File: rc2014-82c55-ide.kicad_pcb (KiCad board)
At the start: 2 copper layers, 100 x 50 mm, 23 parts, among them J1 Conn_01x02, J2 Conn_02x20_Odd_Even, J3 Conn_02x22_Odd_Even, J5 Conn_01x02, P1 Conn_01x39, SW1 SW_DIP_x06, U1 82C55A_PLCC, U2 74HCT688, U3 74HCT04

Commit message: Update PCB components
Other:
- rule pad_to_mask_clearance: 0.2 -> 0
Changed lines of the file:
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@@
   (title_block
     (title "RC2014 82c55 IDE adapter")
-    (date "2022-03-09")
+    (date "2022-10-17")
     (rev "3-pre")
   )
@@
   )
   (setup
-    (pad_to_mask_clearance 0.2)
+    (pad_to_mask_clearance 0)
     (pcbplotparams
       (layerselection 0x00010f0_ffffffff)
@@
     (descr "Through hole straight pin header, 1x39, 2.54mm pitch, single row")
     (tags "Through hole pin header THT 1x39 2.54mm single row")
-    (property "Sheetfile" "rc2014-82c55-ide.kicad_sch")
+    (property "Sheetfile" "File: rc2014-82c55-ide.kicad_sch")
     (property "Sheetname" "")
     (attr through_hole)
@@
     (descr "PLCC, 44 pins, through hole")
     (tags "plcc leaded")
-    (property "Sheetfile" "rc2014-82c55-ide.kicad_sch")
+    (property "Sheetfile" "File: rc2014-82c55-ide.kicad_sch")
     (property "Sheetname" "")
     (attr through_hole)
@@
     (descr "Resistor, Axial_DIN0207 series, Axial, Horizontal, pin pitch=7.62mm, 0.25W = 1/4W, length*diameter=6.3*2.5mm^2, http://cdn-reichelt.de/documents/datenblatt/B400/1_4W%23YAG.pdf")
     (tags "Resistor Axial_DIN0207 series Axial Horizontal pin pitch 7.62mm 0.25W = 1/4W length 6.3mm diameter 2.5mm")
-    (property "Sheetfile" "rc2014-82c55-ide.kicad_sch")
+    (property "Sheetfile" "File: rc2014-82c55-ide.kicad_sch")
     (property "Sheetname" "")
     (attr through_hole)
@@
     (descr "20-lead though-hole mounted DIP package, row spacing 7.62 mm (300 mils), Socket, LongPads")
     (tags "THT DIP DIL PDIP 2.54mm 7.62mm 300mil Socket LongPads")
-    (property "Sheetfile" "rc2014-82c55-ide.kicad_sch")
+    (property "Sheetfile" "File: rc2014-82c55-ide.kicad_sch")
     (property "Sheetname" "")
     (attr through_hole)
@@
     (descr "14-lead though-hole mounted DIP package, row spacing 7.62 mm (300 mils), Socket, LongPads")
     (tags "THT DIP DIL PDIP 2.54mm 7.62mm 300mil Socket LongPads")
-    (property "Sheetfile" "rc2014-82c55-ide.kicad_sch")
+    (property "Sheetfile" "File: rc2014-82c55-ide.kicad_sch")
     (property "Sheetname" "")
     (attr through_hole)
@@
     (descr "Through hole straight pin header, 2x22, 2.00mm pitch, double rows")
     (tags "Through hole pin header THT 2x22 2.00mm double row")
-    (property "Sheetfile" "rc2014-82c55-ide.kicad_sch")
+    (property "Sheetfile" "File: rc2014-82c55-ide.kicad_sch")
     (property "Sheetname" "")
     (attr through_hole)
@@
     (descr "6x-dip-switch SPST , Slide, row spacing 7.62 mm (300 mils), body size 9.78x17.42mm (see e.g. https://www.ctscorp.com/wp-content/uploads/206-208.pdf)")
     (tags "DIP Switch SPST Slide 7.62mm 300mil")
-    (property "Sheetfile" "rc2014-82c55-ide.kicad_sch")
+    (property "Sheetfile" "File: rc2014-82c55-ide.kicad_sch")
     (property "Sheetname" "")
     (attr through_hole)
@@
     (descr "C, Disc series, Radial, pin pitch=2.50mm, , diameter*width=3*2mm^2, Capacitor")
     (tags "C Disc series Radial pin pitch 2.50mm  diameter 3mm width 2mm Capacitor")
-    (property "Sheetfile" "rc2014-82c55-ide.kicad_sch")
+    (property "Sheetfile" "File: rc2014-82c55-ide.kicad_sch")
     (property "Sheetname" "")
     (attr through_hole)
@@
     (descr "C, Disc series, Radial, pin pitch=2.50mm, , diameter*width=3*2mm^2, Capacitor")
     (tags "C Disc series Radial pin pitch 2.50mm  diameter 3mm width 2mm Capacitor")
-    (property "Sheetfile" "rc2014-82c55-ide.kicad_sch")
+    (property "Sheetfile" "File: rc2014-82c55-ide.kicad_sch")
     (property "Sheetname" "")
     (attr through_hole)
@@
     (descr "C, Disc series, Radial, pin pitch=2.50mm, , diameter*width=3*2mm^2, Capacitor")
     (tags "C Disc series Radial pin pitch 2.50mm  diameter 3mm width 2mm Capacitor")
-    (property "Sheetfile" "rc2014-82c55-ide.kicad_sch")
+    (property "Sheetfile" "File: rc2014-82c55-ide.kicad_sch")
     (property "Sheetname" "")
     (attr through_hole)
@@
     (descr "Through hole straight pin header, 2x20, 2.54mm pitch, double rows")
     (tags "Through hole pin header THT 2x20 2.54mm double row")
-    (property "Sheetfile" "rc2014-82c55-ide.kicad_sch")
+    (property "Sheetfile" "File: rc2014-82c55-ide.kicad_sch")
     (property "Sheetname" "")
     (attr through_hole)
@@
     (descr "Through hole straight pin header, 1x02, 2.54mm pitch, single row")
     (tags "Through hole pin header THT 1x02 2.54mm single row")
-    (property "Sheetfile" "rc2014-82c55-ide.kicad_sch")
+    (property "Sheetfile" "File: rc2014-82c55-ide.kicad_sch")
     (property "Sheetname" "")
     (attr through_hole)
@@
     (descr "Through hole straight pin header, 1x03, 2.54mm pitch, single row")
     (tags "Through hole pin header THT 1x03 2.54mm single row")
-    (property "Sheetfile" "rc2014-82c55-ide.kicad_sch")
+    (property "Sheetfile" "File: rc2014-82c55-ide.kicad_sch")
     (property "Sheetname" "")
     (attr through_hole)
@@
     (descr "Through hole straight pin header, 1x03, 2.54mm pitch, single row")
     (tags "Through hole pin header THT 1x03 2.54mm single row")
-    (property "Sheetfile" "rc2014-82c55-ide.kicad_sch")
+    (property "Sheetfile" "File: rc2014-82c55-ide.kicad_sch")
     (property "Sheetname" "")
     (attr through_hole)
@@
     (descr "Through hole straight pin header, 1x03, 2.54mm pitch, single row")
     (tags "Through hole pin header THT 1x03 2.54mm single row")
-    (property "Sheetfile" "rc2014-82c55-ide.kicad_sch")
+    (property "Sheetfile" "File: rc2014-82c55-ide.kicad_sch")
     (property "Sheetname" "")
     (attr through_hole)
@@
     (descr "Through hole straight pin header, 1x03, 2.54mm pitch, single row")
     (tags "Through hole pin header THT 1x03 2.54mm single row")
-    (property "Sheetfile" "rc2014-82c55-ide.kicad_sch")
+    (property "Sheetfile" "File: rc2014-82c55-ide.kicad_sch")
     (property "Sheetname" "")
     (attr through_hole)
@@
     (descr "8-pin Resistor SIP pack")
     (tags "R")
-    (property "Sheetfile" "rc2014-82c55-ide.kicad_sch")
+    (property "Sheetfile" "File: rc2014-82c55-ide.kicad_sch")
     (property "Sheetname" "")
     (attr through_hole)
@@
     (descr "Resistor, Axial_DIN0207 series, Axial, Horizontal, pin pitch=7.62mm, 0.25W = 1/4W, length*diameter=6.3*2.5mm^2, http://cdn-reichelt.de/documents/datenblatt/B400/1_4W%23YAG.pdf")
     (tags "Resistor Axial_DIN0207 series Axial Horizontal pin pitch 7.62mm 0.25W = 1/4W length 6.3mm diameter 2.5mm")
-    (property "Sheetfile" "rc2014-82c55-ide.kicad_sch")
+    (property "Sheetfile" "File: rc2014-82c55-ide.kicad_sch")
     (property "Sheetname" "")
     (attr through_hole)
@@
     (descr "Resistor, Axial_DIN0207 series, Axial, Horizontal, pin pitch=7.62mm, 0.25W = 1/4W, length*diameter=6.3*2.5mm^2, http://cdn-reichelt.de/documents/datenblatt/B400/1_4W%23YAG.pdf")
     (tags "Resistor Axial_DIN0207 series Axial Horizontal pin pitch 7.62mm 0.25W = 1/4W length 6.3mm diameter 2.5mm")
-    (property "Sheetfile" "rc2014-82c55-ide.kicad_sch")
+    (property "Sheetfile" "File: rc2014-82c55-ide.kicad_sch")
     (property "Sheetname" "")
     (attr through_hole)
@@
     (descr "Resistor, Axial_DIN0207 series, Axial, Horizontal, pin pitch=7.62mm, 0.25W = 1/4W, length*diameter=6.3*2.5mm^2, http://cdn-reichelt.de/documents/datenblatt/B400/1_4W%23YAG.pdf")
     (tags "Resistor Axial_DIN0207 series Axial Horizontal pin pitch 7.62mm 0.25W = 1/4W length 6.3mm diameter 2.5mm")
-    (property "Sheetfile" "rc2014-82c55-ide.kicad_sch")
+    (property "Sheetfile" "File: rc2014-82c55-ide.kicad_sch")
     (property "Sheetname" "")
     (attr through_hole)
@@
     (descr "LED, diameter 3.0mm, 2 pins")
     (tags "LED diameter 3.0mm 2 pins")
-    (property "Sheetfile" "rc2014-82c55-ide.kicad_sch")
+    (property "Sheetfile" "File: rc2014-82c55-ide.kicad_sch")
     (property "Sheetname" "")
     (attr through_hole)
@@
     (descr "Through hole straight pin header, 1x02, 2.54mm pitch, single row")
     (tags "Through hole pin header THT 1x02 2.54mm single row")
-    (property "Sheetfile" "rc2014-82c55-ide.kicad_sch")
+    (property "Sheetfile" "File: rc2014-82c55-ide.kicad_sch")
     (property "Sheetname" "")
     (attr through_hole)
@@
     (connect_pads (clearance 0))
     (min_thickness 0.254)
-    (keepout (tracks not_allowed) (vias not_allowed) (pads allowed ) (copperpour allowed) (footprints allowed))
+    (keepout (tracks not_allowed) (vias not_allowed) (pads allowed) (copperpour allowed) (footprints allowed))
     (fill (thermal_gap 0.508) (thermal_bridge_width 0.508))
     (polygon
@@
     (connect_pads (clearance 0))
     (min_thickness 0.254)
-    (keepout (tracks not_allowed) (vias not_allowed) (pads allowed ) (copperpour allowed) (footprints allowed))
+    (keepout (tracks not_allowed) (vias not_allowed) (pads allowed) (copperpour allowed) (footprints allowed))
     (fill (thermal_gap 0.508) (thermal_bridge_width 0.508))
     (polygon
@@
     (connect_pads (clearance 0))
     (min_thickness 0.254)
-    (keepout (tracks allowed) (vias allowed) (pads allowed ) (copperpour not_allowed) (footprints allowed))
+    (keepout (tracks allowed) (vias allowed) (pads allowed) (copperpour not_allowed) (footprints allowed))
     (fill (thermal_gap 0.508) (thermal_bridge_width 0.508))
     (polygon

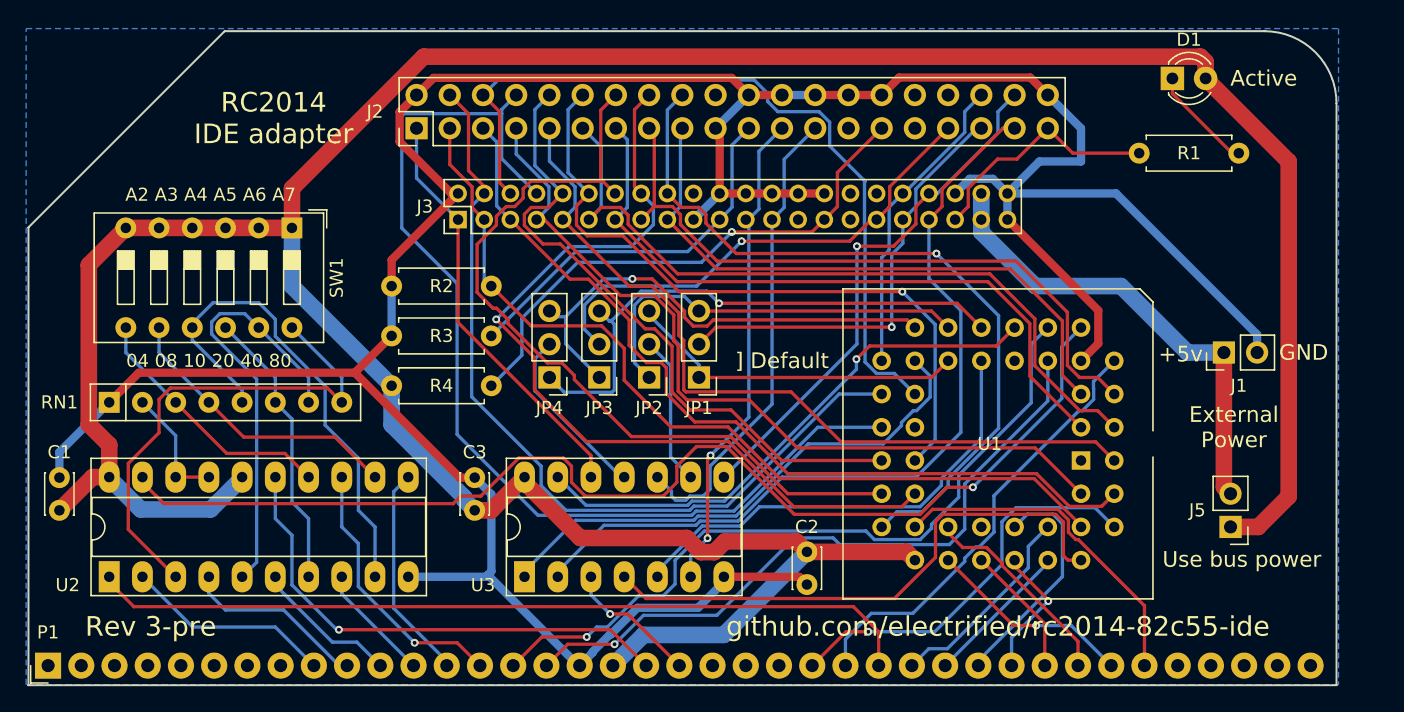
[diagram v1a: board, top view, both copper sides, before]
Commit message: update to kicad 9
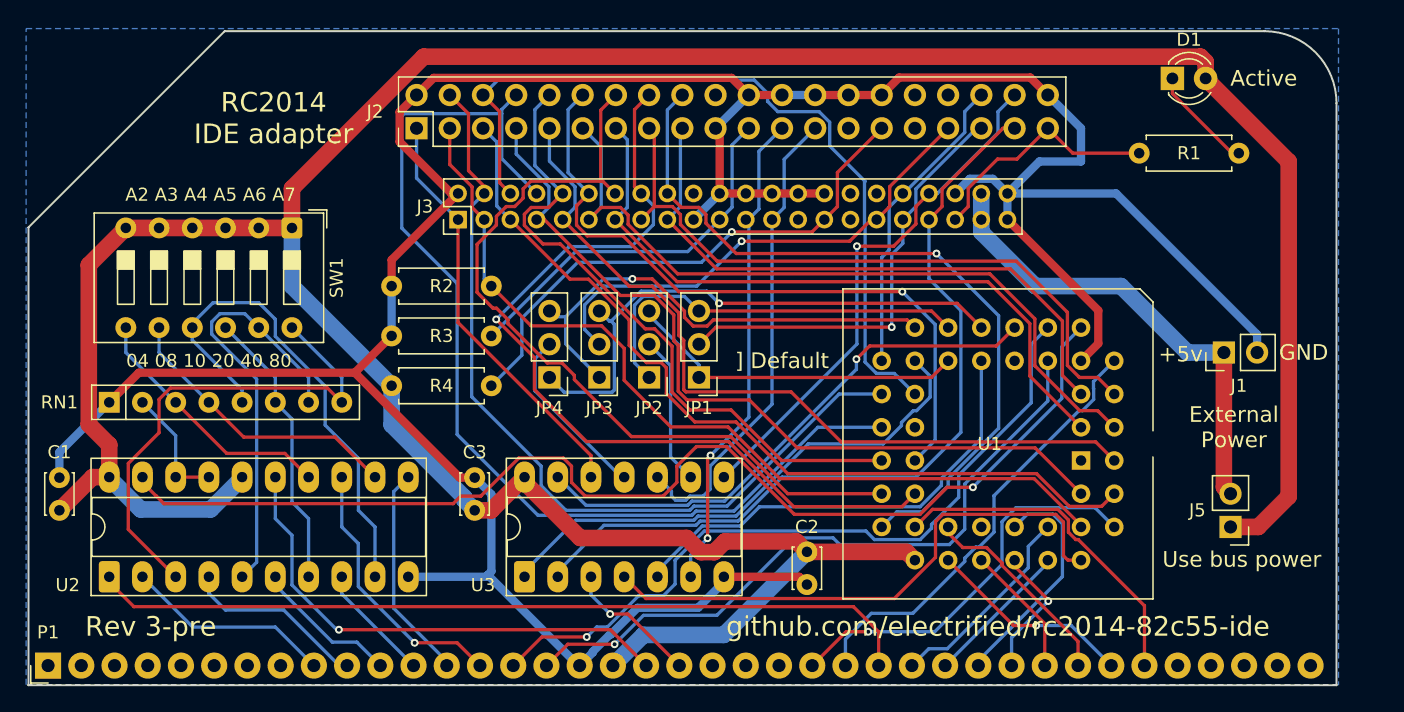
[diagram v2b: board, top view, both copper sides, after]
